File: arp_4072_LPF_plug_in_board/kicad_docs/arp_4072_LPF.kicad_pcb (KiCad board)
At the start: 2 copper layers, 58.4 x 50.8 mm, 80 parts, among them J1 signal_in, J2 CV_in, J3 signal_out, J4 feedback_CV_and_power, Q1 BCM857DS, Q10 MMBT3906, Q2 BCM857DS, Q3 BCM857DS, Q4 BCM857DS, Q5 BCM857DS, Q6 BCM857DS, Q7 BCM847DS135, Q8 MMBT3904, Q9 MMBT3904, U1 LM3900, U2 TL072, U3 TL072

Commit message: change zener value
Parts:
- D1: value 1N5225B -> MMSZ5225B

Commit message: fix schemo and pcb problems
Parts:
- R32: value 470k -> 120k
- R8: value 15k -> 68k
- moved R10 4.46 mm to (152.6, 87.9), turned to 180 degrees
- moved R13 4.19 mm to (156.7, 87.9), turned to 180 degrees
- moved R44 2.92 mm to (154.2, 120.9), turned to 270 degrees
- moved D1 1.92 mm to (151.6, 120.4), turned to 90 degrees
- turned R11 to 90 degrees
- turned R12 to 90 degrees
- turned R18 to 90 degrees
- turned R20 to 270 degrees
- turned R24 to 270 degrees
- turned R25 to 270 degrees
- turned R29 to 270 degrees
- turned R6 to 90 degrees
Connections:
- R10 pad 2: Net-(Q2-Pad6) -> Net-(Q1-Pad6)
- R11 pad 1: /low_pass_core/v_bias -> Net-(Q1-Pad3)
- R11 pad 2: Net-(Q1-Pad3) -> /low_pass_core/v_bias
- R12 pad 1: /low_pass_core/v_bias -> Net-(Q3-Pad2)
- R12 pad 2: Net-(Q3-Pad2) -> /low_pass_core/v_bias
- R13 pad 1: Net-(Q3-Pad6) -> Net-(Q3-Pad2)
- R17 pad 2: Net-(Q3-Pad6) -> Net-(Q3-Pad2)
- R18 pad 1: /low_pass_core/v_bias -> Net-(Q3-Pad5)
- R18 pad 2: Net-(Q3-Pad5) -> /low_pass_core/v_bias
- R20 pad 1: /low_pass_core/v_bias -> Net-(Q5-Pad2)
- R20 pad 2: Net-(Q5-Pad2) -> /low_pass_core/v_bias
- R21 pad 1: Net-(Q5-Pad6) -> Net-(Q5-Pad2)
- R23 pad 2: Net-(Q5-Pad6) -> Net-(Q5-Pad2)
- R24 pad 1: /low_pass_core/v_bias -> Net-(Q5-Pad5)
- R24 pad 2: Net-(Q5-Pad5) -> /low_pass_core/v_bias
- R25 pad 1: /low_pass_core/v_bias -> Net-(Q6-Pad5)
- R25 pad 2: Net-(Q6-Pad5) -> /low_pass_core/v_bias
- R26 pad 1: Net-(Q6-Pad3) -> Net-(Q6-Pad5)
- R28 pad 2: Net-(Q6-Pad3) -> Net-(Q6-Pad5)
- R29 pad 1: /low_pass_core/v_bias -> Net-(Q6-Pad2)
- R29 pad 2: Net-(Q6-Pad2) -> /low_pass_core/v_bias
- R6 pad 1: /low_pass_core/v_bias -> Net-(Q1-Pad6)
- R6 pad 2: Net-(Q1-Pad6) -> /low_pass_core/v_bias
- RV2 pad 3: -12V -> GND
- RV3 pad 1: Net-(D1-Pad1) -> Net-(Q10-Pad2)
- RV3 pad 3: Net-(Q10-Pad2) -> Net-(D1-Pad1)
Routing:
- net -12V: track 174.4 -> 130.4 mm
- net Net-(Q5-Pad2): track 4.48 -> 25.3 mm, vias 0 -> 2
- net Net-(Q3-Pad6): track 32.7 -> 19.0 mm, vias 2 -> 0
- net Net-(Q6-Pad5): track 4.05 -> 17.7 mm
- net Net-(Q3-Pad2): track 4.23 -> 15.0 mm
- net Net-(Q6-Pad3): track 20.3 -> 13.4 mm
- net Net-(Q1-Pad6): track 17.2 -> 22.4 mm
- net Net-(Q5-Pad6): track 15.2 -> 11.3 mm, vias 0 -> 2
- net Net-(C5-Pad1): track 35.8 -> 38.8 mm
- net /feedback_VCA/feedback_CV_in: track 70.2 -> 67.5 mm
- net Net-(C4-Pad1): track 19.1 -> 21.0 mm
- net Net-(Q10-Pad2): track 17.8 -> 19.1 mm, vias 0 -> 1
- net Net-(Q4-Pad3): track 80.7 -> 79.6 mm
- net /low_pass_core/v_bias: track 100.7 -> 101.7 mm
- net Net-(C2-Pad1): track 8.69 -> 8.04 mm
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
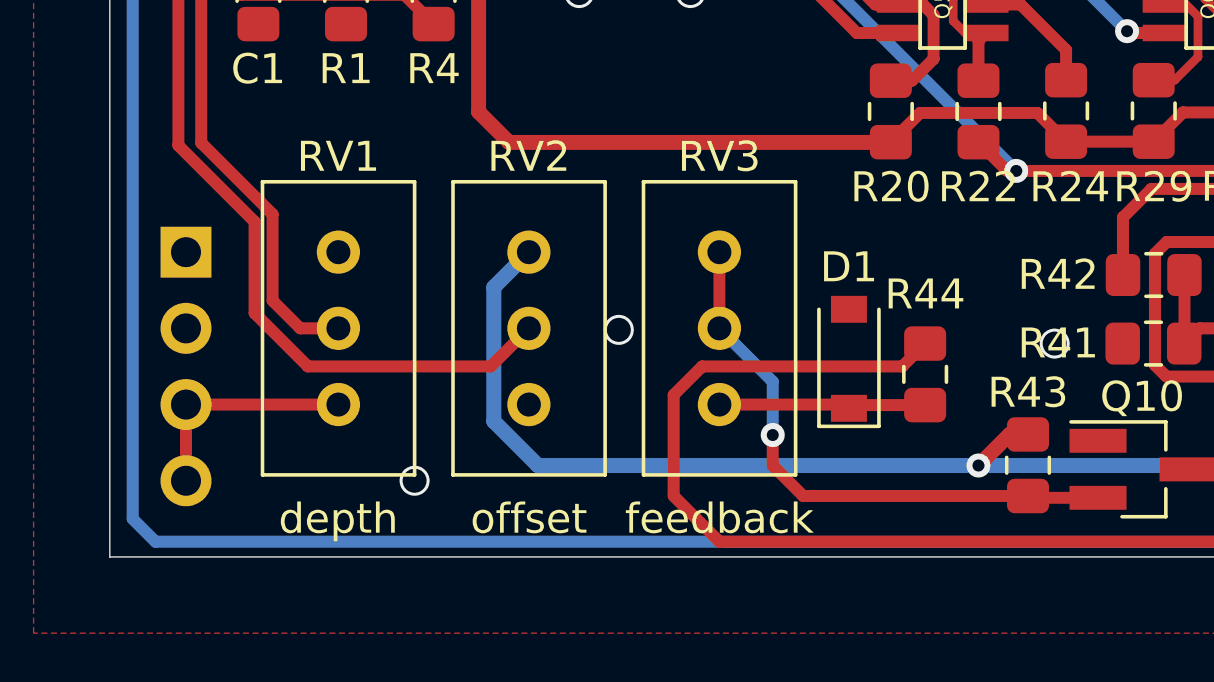
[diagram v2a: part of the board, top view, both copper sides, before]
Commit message: flip trimpots to be consistent with other boards
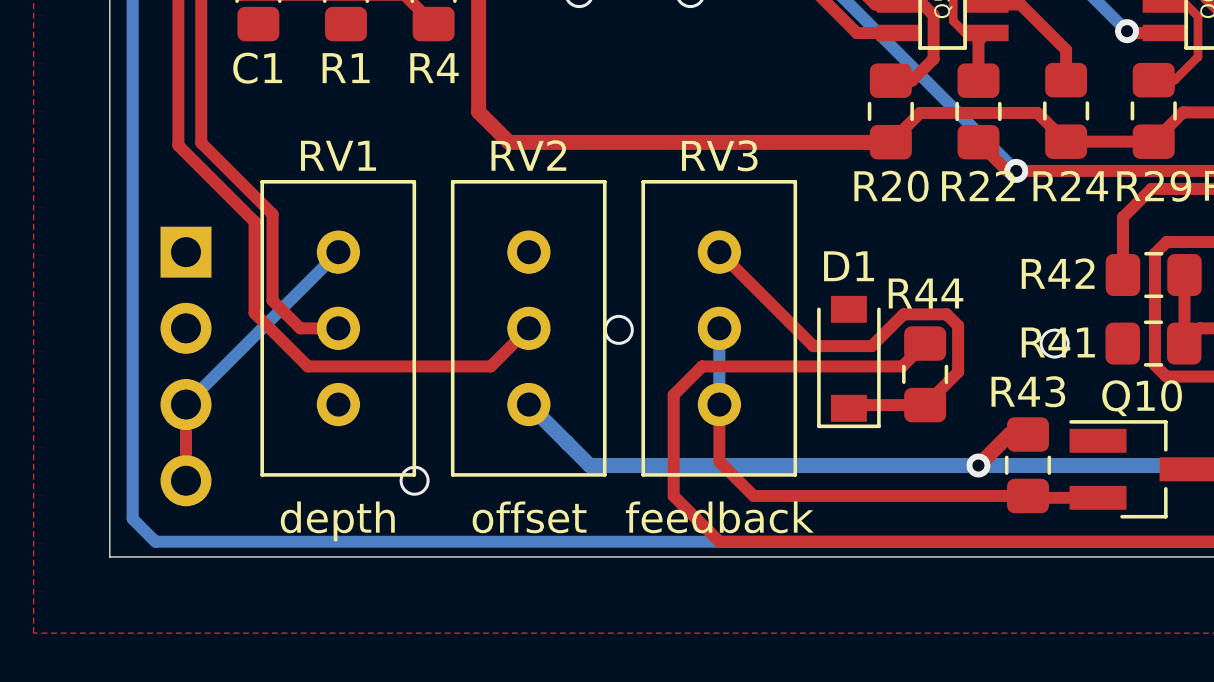
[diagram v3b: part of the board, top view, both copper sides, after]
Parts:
- moved RV1 5.08 mm to (134.6, 121.9), turned to 270 degrees
- moved RV2 5.08 mm to (141.0, 121.9), turned to 270 degrees
- moved RV3 5.08 mm to (147.3, 121.9), turned to 270 degrees
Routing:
- net Net-(D1-Pad1): track 6.95 -> 15.7 mm
- net +12V: track 177.9 -> 170.9 mm
- net /CV_scaler/raw_Vfc_in: track 7.62 -> 9.72 mm
- net Net-(Q10-Pad2): track 19.1 -> 17.6 mm, vias 1 -> 0
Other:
- board text added: "arp_4072_plug_in_board rev 1 2020-08-18"
- board text removed: "arp_4072_plug_in_board rev 0 2020-07-29"
